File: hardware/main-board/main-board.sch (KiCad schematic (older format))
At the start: 48 parts, among them J1 USB_B_Micro, J2 STDC14, SW1 SW_Push, SW2 SW_Push, U1 TCS3472, U2 STM32L052K6U6, U3 AP2502, U4 USBLC6-2SC6, U5 RT9193

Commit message: Added all major components to the schematic
This adds the various new parts needed for the full device, that weren't
on the prototype. It includes another LED driver, more buttons, and a
display interface.

A lot of cleanup is still needed, as well as component designators, MCU
pin assignments, and BOM details.
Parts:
- removed U1: TCS3472, lib_fp:AMS_TCS3472_DFN-6, symbol Project:TCS3472
- added C? (x4): 0.1uF, Capacitor_SMD:C_0603_1608Metric, symbol Device:C_Small
- added C? (x4): 1uF, symbol Device:C_Small
- added C?: 4.7uF, symbol Device:C_Small
- added C?: 2.2uF, symbol Device:C_Small
- added D? (x3): ESDALC6V1-1U2, lib_fp:ST0201, symbol Project:ESDALC6V1-1U2
- added J?: Conn_01x02, symbol Connector_Generic:Conn_01x02
- added J?: Display Connector, lib_fp:ER-CON30HT-1, symbol Project:ER-OLED013
- added R? (x3): 100K, Resistor_SMD:R_0603_1608Metric, symbol Device:R_Small
- added R? (x3): 330R, Resistor_SMD:R_0603_1608Metric, symbol Device:R_Small
- added R?: 390K, symbol Device:R_Small
- added SW3, SW4, SW5: SW_Push, Button_Switch_THT:SW_PUSH_6mm_H5mm, symbol Switch:SW_Push
- added U1: TSL2591, lib_fp:AMS_TSL2591, symbol Project:TSL2591
- added U?: AP2502, Package_TO_SOT_SMD:SOT-23-6, symbol Project:AP2502
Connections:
- net labels added: BTN3, BTN4, BTN5, DISP_RES, RLED_EN, TLED_EN
- net labels removed: LED_EN
- wire segments 133 -> 231
- no-connect marks 24 -> 26
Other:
- note added: "Display Interface"
- note added: "Hinge Button"
- moved on the sheet: C1, C11, C12, C13, C7, C9, D5, D6, D7, D8, H1, H2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

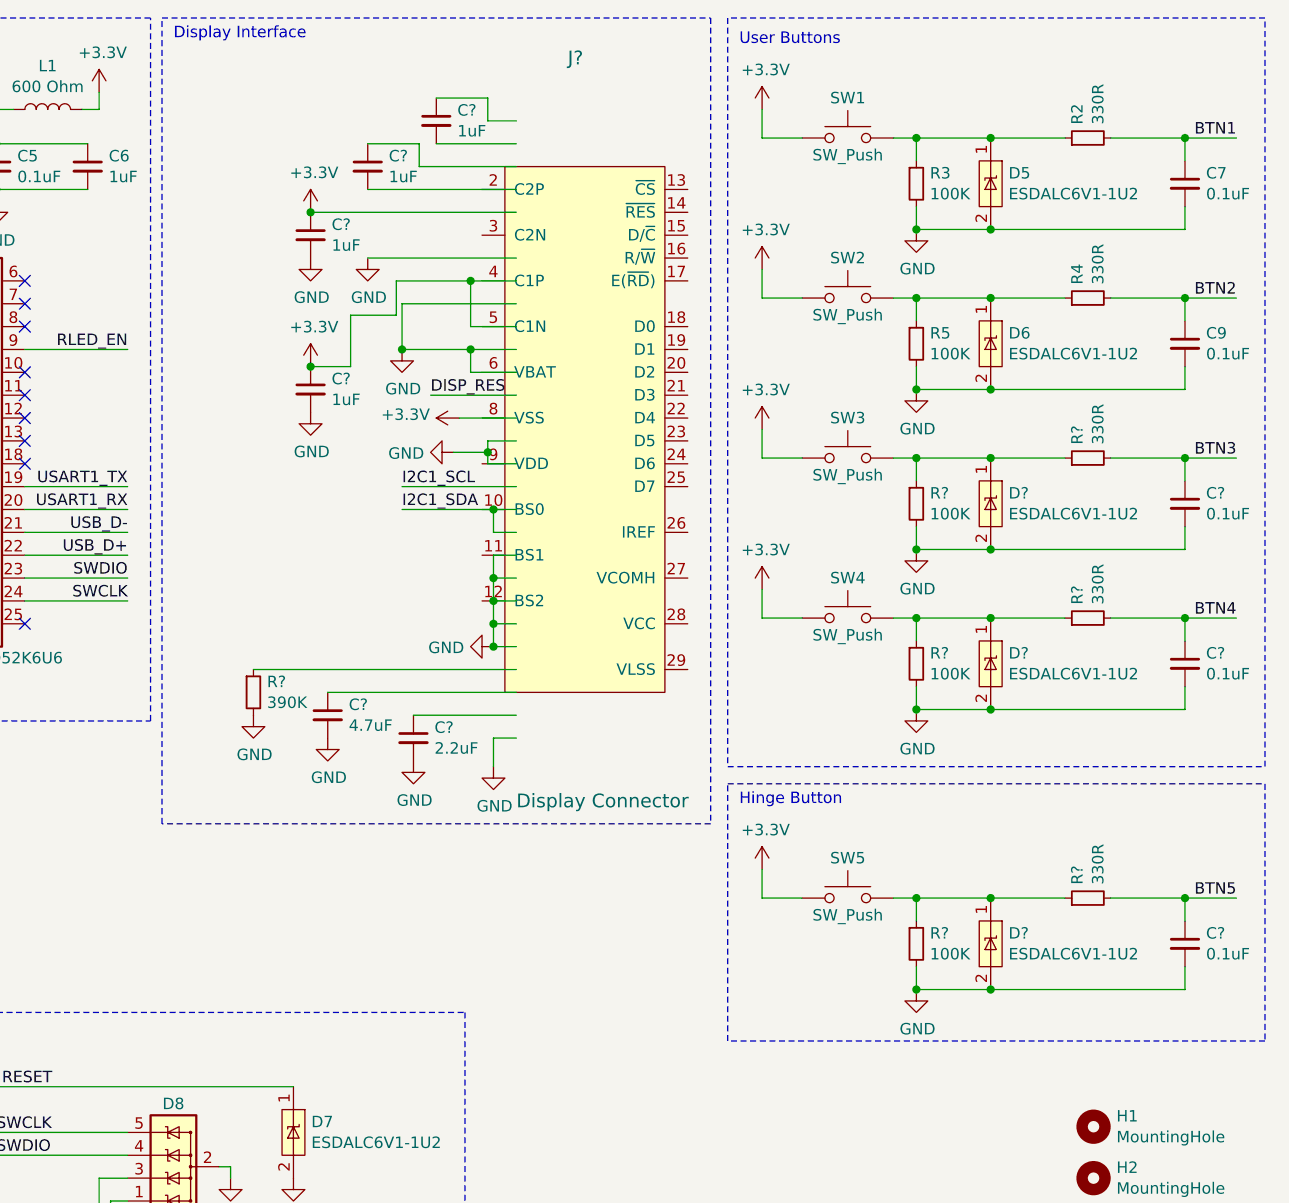
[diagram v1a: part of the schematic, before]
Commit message: Updated display connector symbol for improved layout
This first pass at reorganization is based on the symbols in the
ER-OLED013 interfacing document.
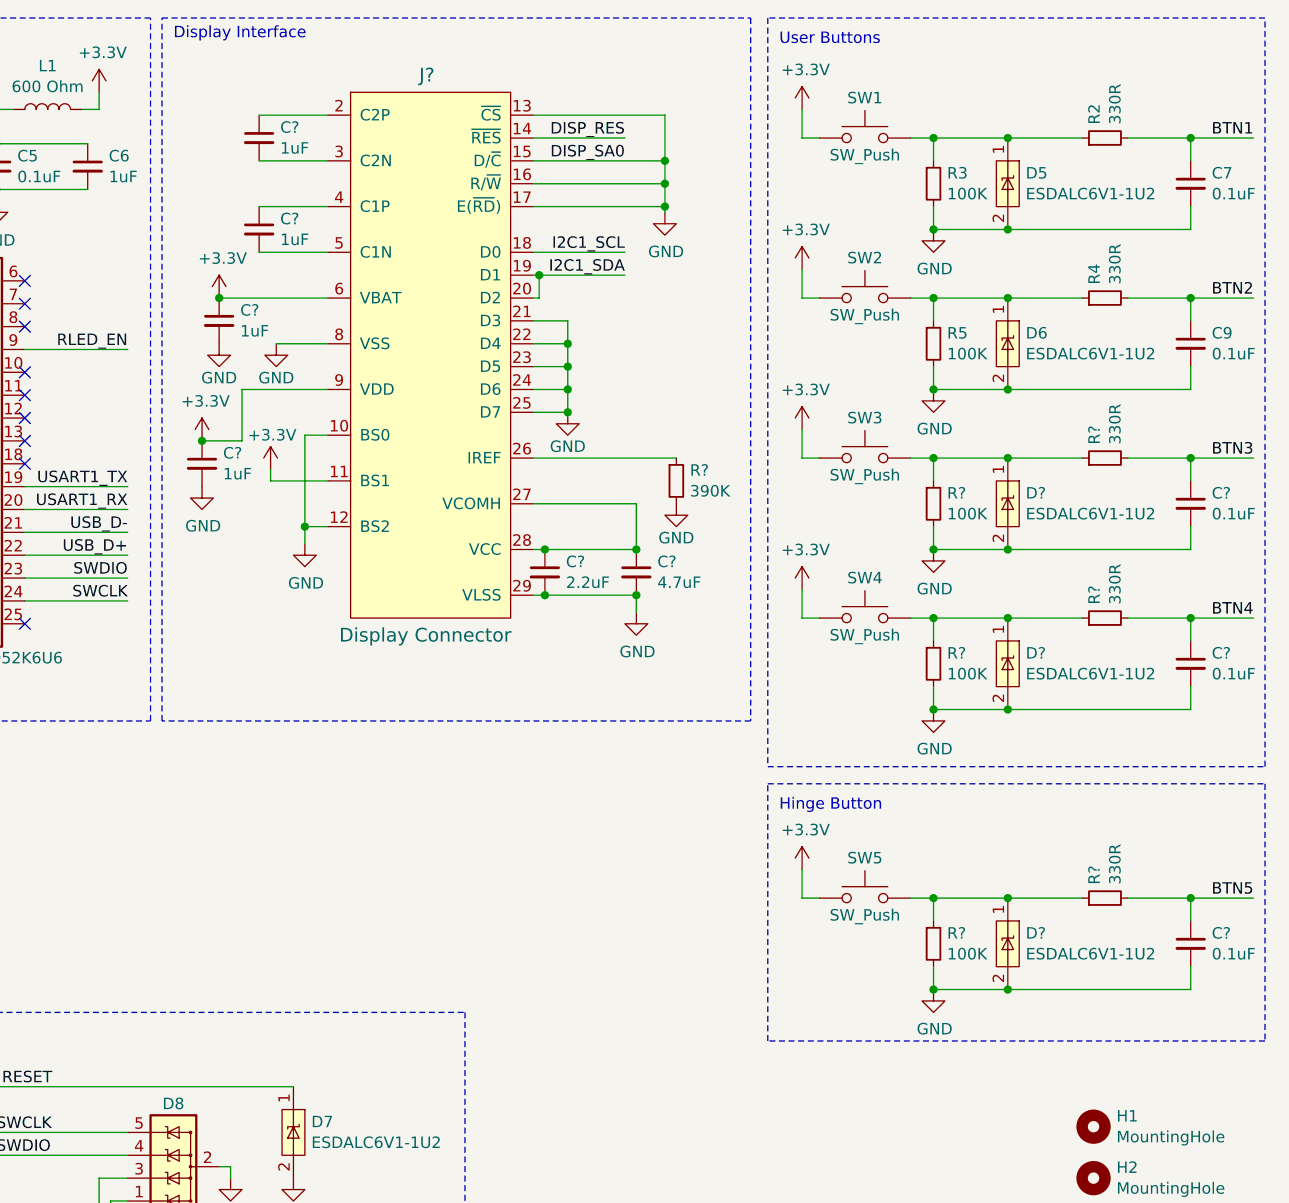
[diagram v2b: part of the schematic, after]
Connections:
- net labels added: DISP_SA0
- wire segments 231 -> 227
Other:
- moved on the sheet: C7, C9, C?, D5, D6, D?, J?, R2, R3, R4, R5, R?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

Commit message: Updated pin assignments and switched display to SPI
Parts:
- added NT1, NT2: Net-Tie_2, symbol Device:Net-Tie_2
- gave numbers to parts that had none: 23
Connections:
- net DISP_RES is gone; now on net DISP_~RES: J3.14 (~RES)
- net +3V3: no longer J3.11 (BS1)
- net BTN1: now also U2.28 (PB5); no longer U2.26 (PB3)
- net BTN3: now also U2.26 (PB3)
- net BTN4: now also U2.25 (PA15)
- net BTN5: now also U2.18 (PA8)
- net GND: now also J3.11 (BS1), NT2.2; no longer J3.13 (~CS), J3.15 (D/~C), J3.21 (D3), J3.22 (D4), J3.23 (D5), J3.24 (D6), J3.25 (D7)
- net I2C1_SCL: no longer J3.18 (D0)
- net I2C1_SDA: no longer J3.19 (D1), J3.20 (D2)
- net RLED_EN: now also U2.8 (PA2); no longer U2.9 (PA3)
- net TLED_EN: now also U2.9 (PA3)
- net DISP_~CS: now reaches U2.10 (PA4)
- net DISP_~CS: now also J3.13 (~CS)
- net DISP_SCK: now reaches U2.11 (PA5)
- net DISP_SCK: now also J3.18 (D0)
- net DISP_D~C: now reaches U2.12 (PA6)
- net DISP_D~C: now also J3.15 (D/~C)
- net DISP_MOSI: now reaches U2.13 (PA7)
- net DISP_MOSI: now also J3.19 (D1)
- net DISP_~RES: now reaches U2.14 (PB0)
- net at J4.2 (Pin_2), U6.6 (LED1): now also NT1.2; no longer U6.5 (LED2)
- new net: NT1.1, U6.5 (LED2)
- new net: J3.21 (D3), J3.22 (D4), J3.23 (D5), J3.24 (D6), J3.25 (D7), NT2.1
- no-connect marks 26 -> 18
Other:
- note added: "Pin assignments subject to change\nduring PCB layout"
- moved on the sheet: C22, J4, R6

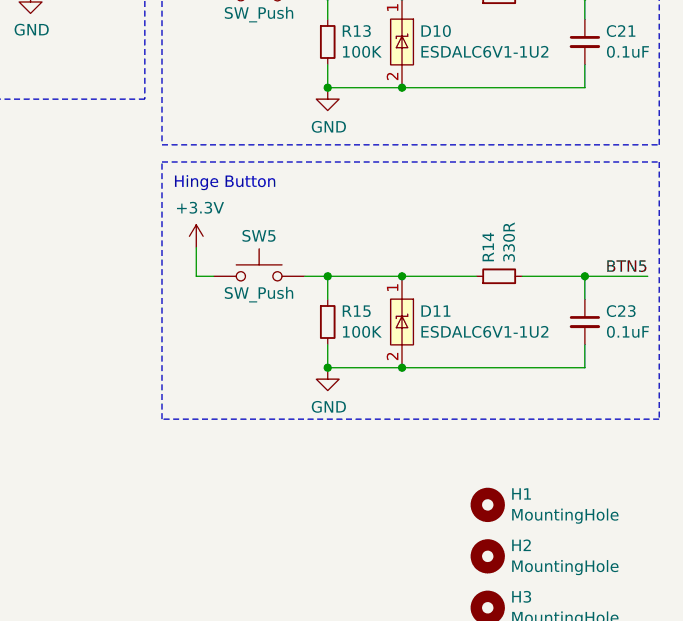
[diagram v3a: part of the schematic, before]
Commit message: Updated switch properties on schematic
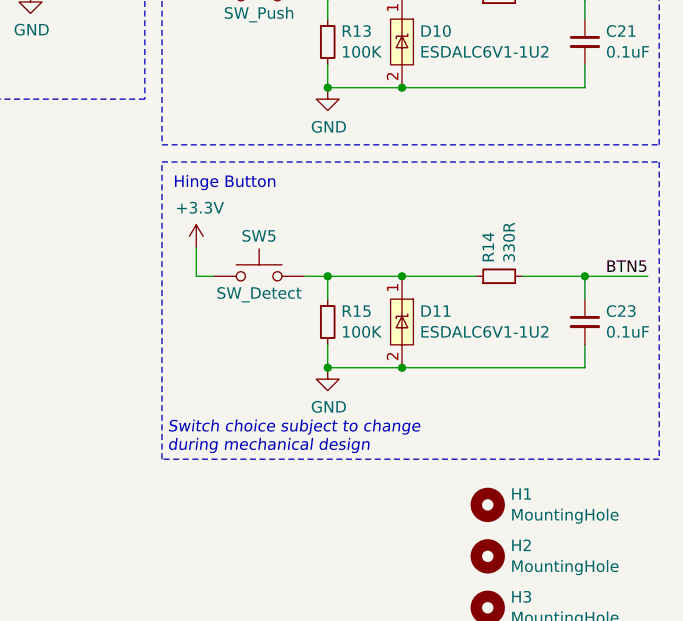
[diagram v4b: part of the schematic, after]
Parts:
- SW1, SW2, SW3, SW4: footprint Button_Switch_THT:SW_PUSH_6mm_H5mm -> lib_fp:ESwitch_TL1105_6mm_H7.5mm; Description SWITCH TACTILE SPST-NO 0.05A 24V -> SWITCH TACTILE SPST-NO 0.05A 12V; Manufacturer Omron Electronics Inc -> E-Switch; Manufacturer PN B3F-1020 -> TL1105SPF160Q; Supplier PN SW402-ND -> EG1861-ND
- SW5: value SW_Push -> SW_Detect; footprint Button_Switch_THT:SW_PUSH_6mm_H5mm -> lib_fp:CK_KSU213WLFG; Description SWITCH TACTILE SPST-NO 0.05A 24V -> SWITCH DETECTOR SPST-NO 10MA 50V; Manufacturer Omron Electronics Inc -> C&K; Manufacturer PN B3F-1020 -> KSU213WLFG; Supplier PN SW402-ND -> 401-1598-1-ND
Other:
- note added: "Switch choice subject to change\nduring mechanical design"
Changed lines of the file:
@@
 F 0 "SW1" H 8700 1250 50  0000 C CNN
 F 1 "SW_Push" H 8700 1000 50  0000 C CNN
-F 2 "Button_Switch_THT:SW_PUSH_6mm_H5mm" H 8700 1275 50  0001 C CNN
-F 3 "https://omronfs.omron.com/en_US/ecb/products/pdf/en-b3f.pdf" H 8700 1275 50  0001 C CNN
-F 4 "SWITCH TACTILE SPST-NO 0.05A 24V" H 8700 1075 50  0001 C CNN "Description"
-F 5 "Omron Electronics Inc" H 8700 1075 50  0001 C CNN "Manufacturer"
-F 6 "B3F-1020" H 8700 1075 50  0001 C CNN "Manufacturer PN"
+F 2 "lib_fp:ESwitch_TL1105_6mm_H7.5mm" H 8700 1275 50  0001 C CNN
+F 3 "https://www.e-switch.com/system/asset/product_line/data_sheet/144/TL1105.pdf" H 8700 1275 50  0001 C CNN
+F 4 "SWITCH TACTILE SPST-NO 0.05A 12V" H 8700 1075 50  0001 C CNN "Description"
+F 5 "E-Switch" H 8700 1075 50  0001 C CNN "Manufacturer"
+F 6 "TL1105SPF160Q" H 8700 1075 50  0001 C CNN "Manufacturer PN"
 F 7 "Digi-Key" H 8700 1075 50  0001 C CNN "Supplier"
-F 8 "SW402-ND" H 8700 1075 50  0001 C CNN "Supplier PN"
+F 8 "EG1861-ND" H 8700 1075 50  0001 C CNN "Supplier PN"
 	1    8700 1075
 	1    0    0    -1
@@
 F 0 "SW2" H 8700 1950 50  0000 C CNN
 F 1 "SW_Push" H 8700 1700 50  0000 C CNN
-F 2 "Button_Switch_THT:SW_PUSH_6mm_H5mm" H 8700 1975 50  0001 C CNN
-F 3 "https://omronfs.omron.com/en_US/ecb/products/pdf/en-b3f.pdf" H 8700 1975 50  0001 C CNN
-F 4 "SWITCH TACTILE SPST-NO 0.05A 24V" H 8700 1775 50  0001 C CNN "Description"
-F 5 "Omron Electronics Inc" H 8700 1775 50  0001 C CNN "Manufacturer"
-F 6 "B3F-1020" H 8700 1775 50  0001 C CNN "Manufacturer PN"
+F 2 "lib_fp:ESwitch_TL1105_6mm_H7.5mm" H 8700 1975 50  0001 C CNN
+F 3 "https://www.e-switch.com/system/asset/product_line/data_sheet/144/TL1105.pdf" H 8700 1975 50  0001 C CNN
+F 4 "SWITCH TACTILE SPST-NO 0.05A 12V" H 8700 1775 50  0001 C CNN "Description"
+F 5 "E-Switch" H 8700 1775 50  0001 C CNN "Manufacturer"
+F 6 "TL1105SPF160Q" H 8700 1775 50  0001 C CNN "Manufacturer PN"
 F 7 "Digi-Key" H 8700 1775 50  0001 C CNN "Supplier"
-F 8 "SW402-ND" H 8700 1775 50  0001 C CNN "Supplier PN"
+F 8 "EG1861-ND" H 8700 1775 50  0001 C CNN "Supplier PN"
 	1    8700 1775
 	1    0    0    -1
@@
 F 0 "SW3" H 8700 2650 50  0000 C CNN
 F 1 "SW_Push" H 8700 2400 50  0000 C CNN
-F 2 "Button_Switch_THT:SW_PUSH_6mm_H5mm" H 8700 2675 50  0001 C CNN
-F 3 "https://omronfs.omron.com/en_US/ecb/products/pdf/en-b3f.pdf" H 8700 2675 50  0001 C CNN
-F 4 "SWITCH TACTILE SPST-NO 0.05A 24V" H 8700 2475 50  0001 C CNN "Description"
-F 5 "Omron Electronics Inc" H 8700 2475 50  0001 C CNN "Manufacturer"
-F 6 "B3F-1020" H 8700 2475 50  0001 C CNN "Manufacturer PN"
+F 2 "lib_fp:ESwitch_TL1105_6mm_H7.5mm" H 8700 2675 50  0001 C CNN
+F 3 "https://www.e-switch.com/system/asset/product_line/data_sheet/144/TL1105.pdf" H 8700 2675 50  0001 C CNN
+F 4 "SWITCH TACTILE SPST-NO 0.05A 12V" H 8700 2475 50  0001 C CNN "Description"
+F 5 "E-Switch" H 8700 2475 50  0001 C CNN "Manufacturer"
+F 6 "TL1105SPF160Q" H 8700 2475 50  0001 C CNN "Manufacturer PN"
 F 7 "Digi-Key" H 8700 2475 50  0001 C CNN "Supplier"
-F 8 "SW402-ND" H 8700 2475 50  0001 C CNN "Supplier PN"
+F 8 "EG1861-ND" H 8700 2475 50  0001 C CNN "Supplier PN"
 	1    8700 2475
 	1    0    0    -1
@@
 F 0 "SW4" H 8700 3350 50  0000 C CNN
 F 1 "SW_Push" H 8700 3100 50  0000 C CNN
-F 2 "Button_Switch_THT:SW_PUSH_6mm_H5mm" H 8700 3375 50  0001 C CNN
-F 3 "https://omronfs.omron.com/en_US/ecb/products/pdf/en-b3f.pdf" H 8700 3375 50  0001 C CNN
-F 4 "SWITCH TACTILE SPST-NO 0.05A 24V" H 8700 3175 50  0001 C CNN "Description"
-F 5 "Omron Electronics Inc" H 8700 3175 50  0001 C CNN "Manufacturer"
-F 6 "B3F-1020" H 8700 3175 50  0001 C CNN "Manufacturer PN"
+F 2 "lib_fp:ESwitch_TL1105_6mm_H7.5mm" H 8700 3375 50  0001 C CNN
+F 3 "https://www.e-switch.com/system/asset/product_line/data_sheet/144/TL1105.pdf" H 8700 3375 50  0001 C CNN
+F 4 "SWITCH TACTILE SPST-NO 0.05A 12V" H 8700 3175 50  0001 C CNN "Description"
+F 5 "E-Switch" H 8700 3175 50  0001 C CNN "Manufacturer"
+F 6 "TL1105SPF160Q" H 8700 3175 50  0001 C CNN "Manufacturer PN"
 F 7 "Digi-Key" H 8700 3175 50  0001 C CNN "Supplier"
-F 8 "SW402-ND" H 8700 3175 50  0001 C CNN "Supplier PN"
+F 8 "EG1861-ND" H 8700 3175 50  0001 C CNN "Supplier PN"
 	1    8700 3175
 	1    0    0    -1
@@
 P 8700 4400
 F 0 "SW5" H 8700 4575 50  0000 C CNN
-F 1 "SW_Push" H 8700 4325 50  0000 C CNN
-F 2 "Button_Switch_THT:SW_PUSH_6mm_H5mm" H 8700 4600 50  0001 C CNN
-F 3 "https://omronfs.omron.com/en_US/ecb/products/pdf/en-b3f.pdf" H 8700 4600 50  0001 C CNN
-F 4 "SWITCH TACTILE SPST-NO 0.05A 24V" H 8700 4400 50  0001 C CNN "Description"
-F 5 "Omron Electronics Inc" H 8700 4400 50  0001 C CNN "Manufacturer"
-F 6 "B3F-1020" H 8700 4400 50  0001 C CNN "Manufacturer PN"
+F 1 "SW_Detect" H 8700 4325 50  0000 C CNN
+F 2 "lib_fp:CK_KSU213WLFG" H 8700 4600 50  0001 C CNN
+F 3 "https://www.ckswitches.com/media/1312/ksu.pdf" H 8700 4600 50  0001 C CNN
+F 4 "SWITCH DETECTOR SPST-NO 10MA 50V" H 8700 4400 50  0001 C CNN "Description"
+F 5 "C&K" H 8700 4400 50  0001 C CNN "Manufacturer"
+F 6 "KSU213WLFG" H 8700 4400 50  0001 C CNN "Manufacturer PN"
 F 7 "Digi-Key" H 8700 4400 50  0001 C CNN "Supplier"
-F 8 "SW402-ND" H 8700 4400 50  0001 C CNN "Supplier PN"
+F 8 "401-1598-1-ND" H 8700 4400 50  0001 C CNN "Supplier PN"
 	1    8700 4400
 	1    0    0    -1
@@
 	8275 3900 10450 3900
 Wire Notes Line
-	10450 3900 10450 5025
-Wire Notes Line
-	10450 5025 8275 5025
-Wire Notes Line
-	8275 5025 8275 3900
+	10450 3900 10450 5200
+Wire Notes Line
+	10450 5200 8275 5200
+Wire Notes Line
+	8275 5200 8275 3900
 $Comp
 L Device:C_Small C14
@@
 Wire Wire Line
 	3525 2400 3925 2400
+Text Notes 8300 5175 0    50   Italic 0
+Switch choice subject to change\nduring mechanical design
 $EndSCHEMATC
